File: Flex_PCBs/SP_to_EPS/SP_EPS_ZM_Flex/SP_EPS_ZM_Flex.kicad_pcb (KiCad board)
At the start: 2 copper layers, 4.5 x 55 mm, 2 parts, among them J1 Conn_01x08_Male, J2 Conn_01x08_Male

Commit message: Add SP EPS ZM
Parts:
- moved J1 5.08 mm to (120.0, 54.0)
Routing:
- net 6: track 50.9 -> 56.0 mm
- net 8: track 50.8 -> 55.9 mm
- net 7: track 50.9 -> 56.0 mm
- net 5: track 50.8 -> 55.9 mm
- net 4: track 51.0 -> 56.1 mm
- net 3: track 50.9 -> 56.0 mm
- net 2: track 51.0 -> 56.1 mm
- net 1: track 50.9 -> 56.0 mm
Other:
- board size 4.5 x 55 mm -> 4.5 x 60 mm
- board text added: "SP_EPS_ZM_Flex FM V1.0"
- board text removed: "SP_EPS_ZP_Flex FM V1.0"
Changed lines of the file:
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@@
 	(footprint "STS_connector:flexpcb con."
 		(layer "F.Cu")
-		(at 119.9718 59.0836)
+		(at 119.9718 54)
 		(property "Reference" "J1"
 			(at -16.51 -3.81 0)
@@
 	)
 	(gr_line
-		(start 120 55)
+		(start 120 50)
 		(end 120 110)
 		(stroke
@@
 	)
 	(gr_line
-		(start 120 55)
-		(end 124.5 55)
+		(start 120 50)
+		(end 124.5 50)
 		(stroke
 			(width 0.1)
@@
 	)
 	(gr_line
-		(start 124.5 55)
+		(start 124.5 50)
 		(end 124.5 110)
 		(stroke
@@
 	)
 	(gr_rect
-		(start 120 55)
-		(end 124.5 64.26)
+		(start 120 50)
+		(end 124.5 59.26)
 		(stroke
 			(width 0.15)
@@
 		(layer "User.1")
 	)
-	(gr_text "SP_EPS_ZP_Flex FM V1.0"
+	(gr_text "SP_EPS_ZM_Flex FM V1.0"
 		(at 121.4318 99.2436 90)
 		(layer "F.SilkS")
@@
 		(layer "User.1")
 		(pts
-			(xy 120 55) (xy 120 64.26)
+			(xy 120 50) (xy 120 59.26)
 		)
 		(height 1.499999)
 		(gr_text "9,2600 mm"
-			(at 117.350001 59.63 90)
+			(at 117.350001 54.63 90)
 			(layer "User.1")
 			(effects
@@
 		(layer "User.1")
 		(pts
-			(xy 120 55) (xy 124.5 55)
+			(xy 120 50) (xy 124.5 50)
 		)
 		(height -4)
 		(gr_text "4,5000 mm"
-			(at 122.25 49.85 0)
+			(at 122.25 44.85 0)
 			(layer "User.1")
 			(effects
@@
 		(layer "User.1")
 		(pts
-			(xy 120 55) (xy 120 110)
+			(xy 120 50) (xy 120 110)
 		)
 		(height 5.999999)
-		(gr_text "55,0000 mm"
-			(at 112.850001 82.5 90)
+		(gr_text "60,0000 mm"
+			(at 112.850001 80 90)
 			(layer "User.1")
 			(effects
@@
 	)
 	(segment
-		(start 120.4718 104.2112)
-		(end 120.4718 57.0836)
-		(width 0.25)
-		(layer "F.Cu")
-		(net 1)
-	)
-	(segment
 		(start 120.5 104.2394)
 		(end 120.4718 104.2112)
+		(width 0.25)
+		(layer "F.Cu")
+		(net 1)
+	)
+	(segment
+		(start 120.4718 104.2112)
+		(end 120.4718 52)
 		(width 0.25)
 		(layer "F.Cu")
@@
 	)
 	(segment
+		(start 120.9718 52)
+		(end 120.9718 103.8128)
+		(width 0.25)
+		(layer "F.Cu")
+		(net 2)
+	)
+	(segment
 		(start 120.9718 103.8128)
 		(end 121.0254 103.8664)
-		(width 0.25)
-		(layer "F.Cu")
-		(net 2)
-	)
-	(segment
-		(start 120.9718 57.0836)
-		(end 120.9718 103.8128)
 		(width 0.25)
 		(layer "F.Cu")
@@
 	)
 	(segment
-		(start 121.4718 57.0836)
+		(start 121.4718 52)
 		(end 121.4718 103.2968)
 		(width 0.25)
@@
 	)
 	(segment
+		(start 121.5 103.325)
+		(end 121.5334 103.3584)
+		(width 0.25)
+		(layer "F.Cu")
+		(net 3)
+	)
+	(segment
 		(start 121.4718 103.2968)
-		(end 121.5334 103.3584)
-		(width 0.25)
-		(layer "F.Cu")
-		(net 3)
-	)
-	(segment
-		(start 121.5 103.325)
 		(end 121.5334 103.3584)
 		(width 0.25)
@@
 	)
 	(segment
-		(start 121.9718 57.0836)
-		(end 121.9718 102.9586)
-		(width 0.25)
-		(layer "F.Cu")
-		(net 4)
-	)
-	(segment
 		(start 121.9718 102.9586)
 		(end 122.0414 103.0282)
+		(width 0.25)
+		(layer "F.Cu")
+		(net 4)
+	)
+	(segment
+		(start 121.9718 52)
+		(end 121.9718 102.9586)
 		(width 0.25)
 		(layer "F.Cu")
@@
 	)
 	(segment
+		(start 122.4718 52)
+		(end 122.4718 102.595)
+		(width 0.25)
+		(layer "F.Cu")
+		(net 5)
+	)
+	(segment
 		(start 122.5 102.5442)
 		(end 122.4986 102.5456)
@@
 	)
 	(segment
-		(start 122.4718 57.0836)
-		(end 122.4718 102.595)
+		(start 122.4718 102.595)
+		(end 122.5494 102.6726)
 		(width 0.25)
 		(layer "F.Cu")
@@
 	(segment
 		(start 122.4986 102.6218)
-		(end 122.5494 102.6726)
-		(width 0.25)
-		(layer "F.Cu")
-		(net 5)
-	)
-	(segment
-		(start 122.4718 102.595)
 		(end 122.5494 102.6726)
 		(width 0.25)
@@
 	)
 	(segment
-		(start 122.9718 57.0836)
+		(start 122.9718 52)
 		(end 122.9718 102.2314)
 		(width 0.25)
@@
 	)
 	(segment
+		(start 123 102.2596)
+		(end 123.032 102.2916)
+		(width 0.25)
+		(layer "F.Cu")
+		(net 6)
+	)
+	(segment
 		(start 122.9718 102.2314)
-		(end 123.032 102.2916)
-		(width 0.25)
-		(layer "F.Cu")
-		(net 6)
-	)
-	(segment
-		(start 123 102.2596)
 		(end 123.032 102.2916)
 		(width 0.25)
@@
 	)
 	(segment
-		(start 123.4718 57.0836)
-		(end 123.4718 101.8932)
+		(start 123.4718 101.8932)
+		(end 123.54 101.9614)
 		(width 0.25)
 		(layer "F.Cu")
@@
 	)
 	(segment
-		(start 123.4718 101.8932)
-		(end 123.54 101.9614)
+		(start 123.4718 52)
+		(end 123.4718 101.8932)
 		(width 0.25)
 		(layer "F.Cu")
@@
 	)
 	(segment
-		(start 123.9718 57.0836)
-		(end 123.9718 101.5804)
-		(width 0.25)
-		(layer "F.Cu")
-		(net 8)
-	)
-	(segment
 		(start 123.9718 101.5804)
 		(end 124.0734 101.682)
 		(width 0.25)
 		(layer "F.Cu")
+		(net 8)
+	)
+	(segment
+		(start 123.9718 52)
+		(end 123.9718 101.5804)
+		(width 0.25)
+		(layer "F.Cu")

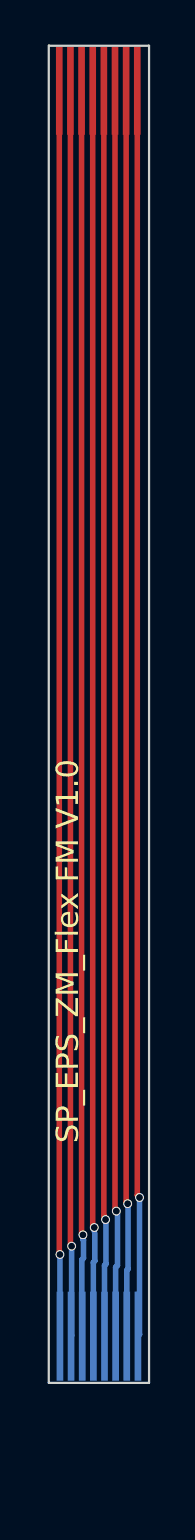
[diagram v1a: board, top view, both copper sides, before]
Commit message: Update the EPS FlexPCBs, with correct top/down and crossed out
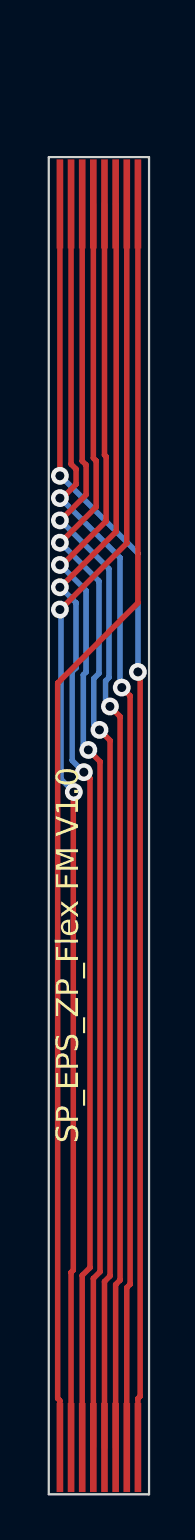
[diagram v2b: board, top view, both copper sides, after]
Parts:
- J2: moved to F.Cu
- moved J2 6.72 mm to (120.0, 114.9), turned to 0 degrees
- moved J1 5.10 mm to (120.0, 59.1)
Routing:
- net 5: track 55.9 -> 57.8 mm, vias 1 -> 2
- net 3: track 56.0 -> 57.7 mm, vias 1 -> 2
- net 6: track 56.0 -> 57.7 mm, vias 1 -> 2
- net 7: track 56.0 -> 57.6 mm, vias 1 -> 2
- net 4: track 56.1 -> 57.7 mm, vias 1 -> 2
- net 8: track 55.9 -> 57.3 mm, vias 1 -> 2
- net 1: track 56.0 -> 57.3 mm, vias 1 -> 0
- net 2: track 56.1 -> 57.4 mm, vias 1 -> 2
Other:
- board text added: "SP_EPS_ZP_Flex FM V1.0"
- board text removed: "SP_EPS_ZM_Flex FM V1.0"
